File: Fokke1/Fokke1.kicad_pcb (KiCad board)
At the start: 2 copper layers, 209 x 64 mm, 97 parts, among them J1 Conn_02x20_Top_Bottom, SW1 SW_SPST, SW10 SW_SPST, SW11 SW_SPST, SW12 SW_SPST, SW2 SW_SPST, SW3 SW_SPST, SW4 SW_SPST, SW5 SW_SPST, SW6 SW_SPST, SW7 SW_SPST, SW8 SW_SPST, SW9 SW_SPST

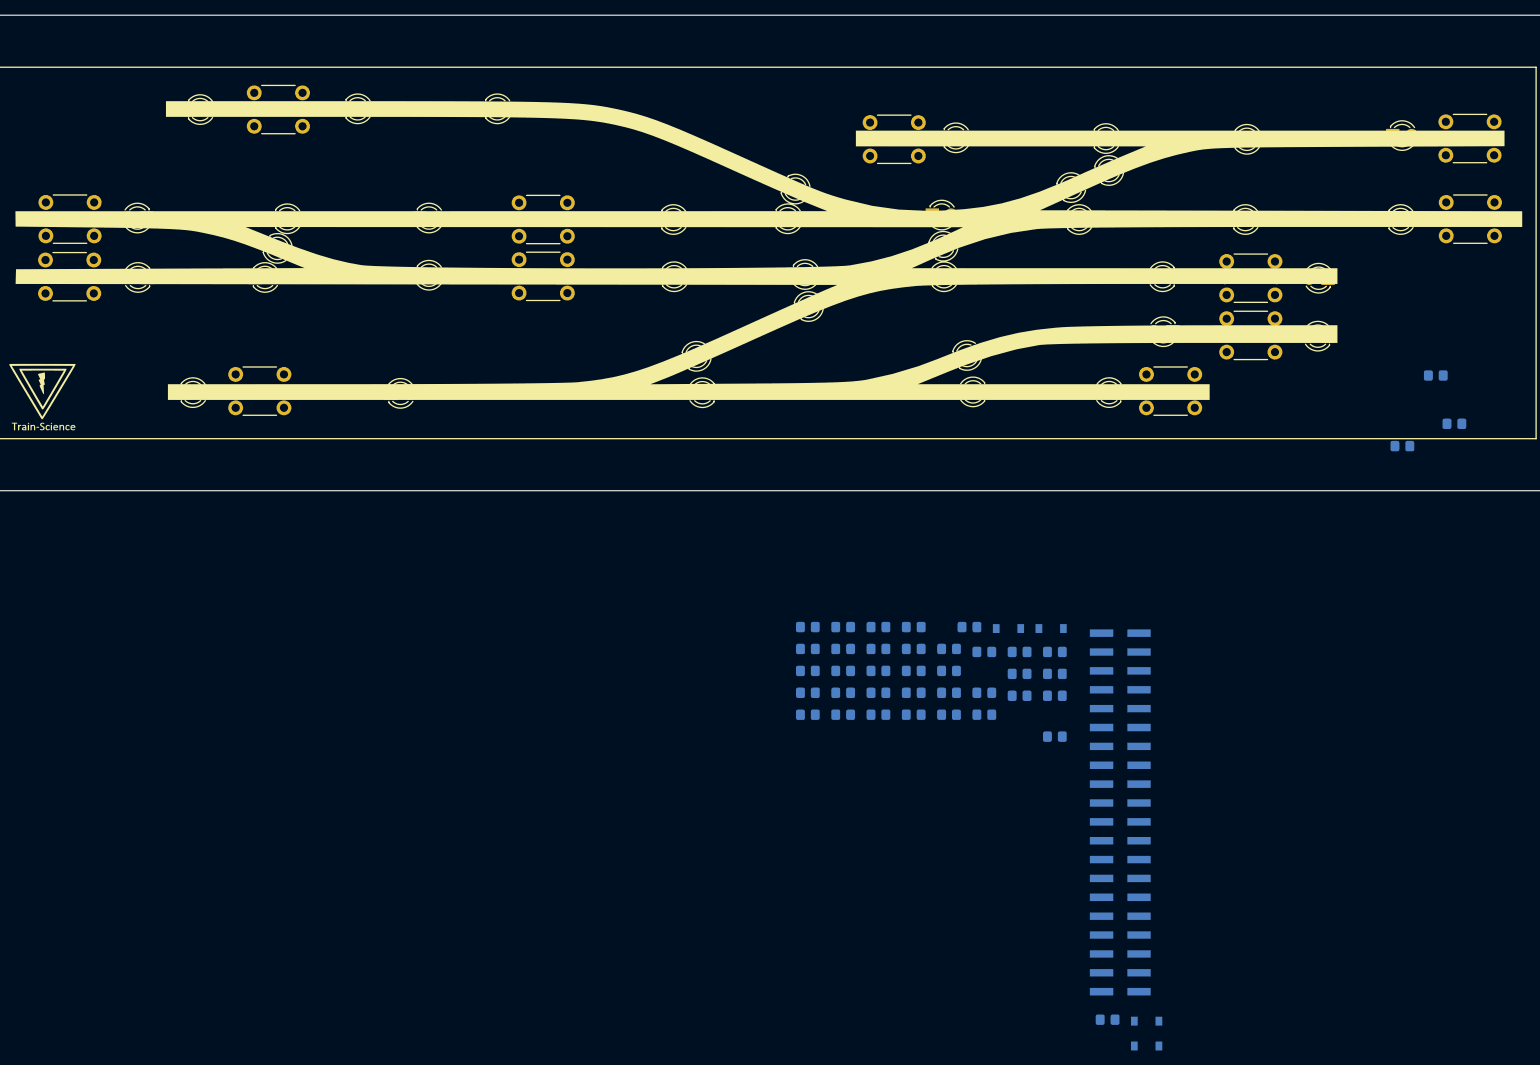
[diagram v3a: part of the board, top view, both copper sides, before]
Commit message: routed all but the main connector of Fokke1
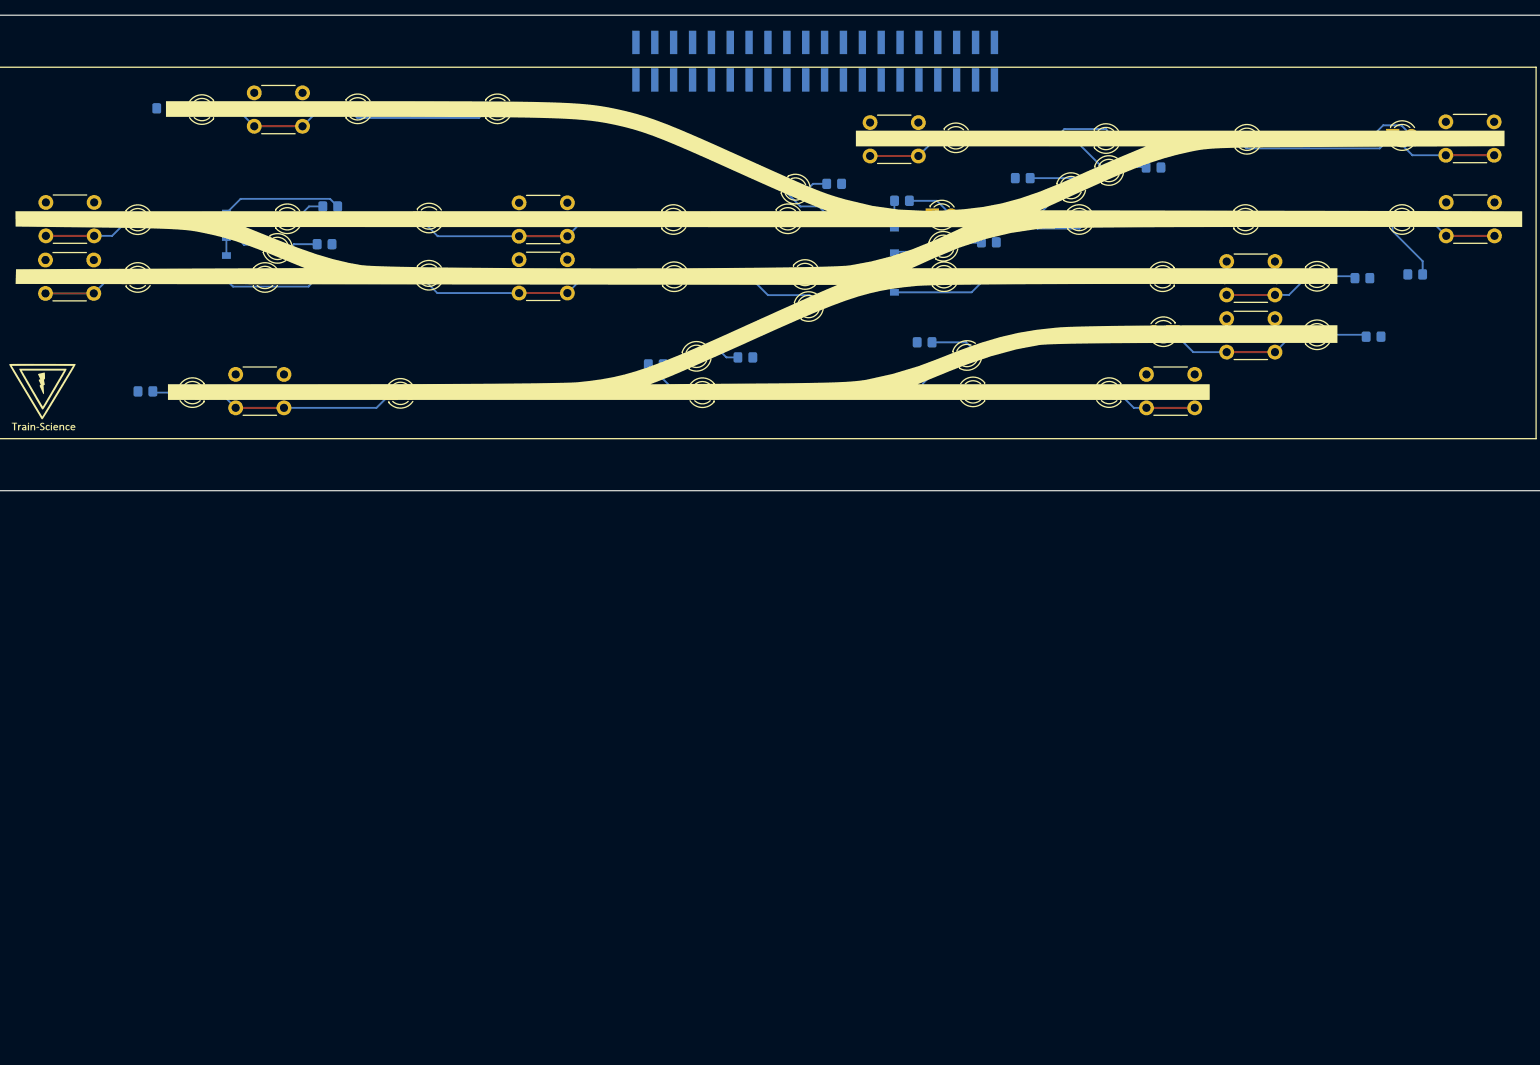
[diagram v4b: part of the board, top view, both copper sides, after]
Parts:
- moved R1 173.8 mm to (54.4, 96.5)
- moved D4 160.1 mm to (60.7, 103.0), turned to 90 degrees
- moved R31 126.2 mm to (52.3, 81.5), turned to 0 degrees
- moved R2 123.1 mm to (54.6, 104.4)
- moved R132 120.9 mm to (74.7, 94.7)
- moved D3 118.4 mm to (60.7, 97.3), turned to -90 degrees
- moved J1 109.1 mm to (140.0, 75.2), turned to -90 degrees
- moved D6 108.6 mm to (150.6, 104.6), turned to 90 degrees
- moved R152 105.0 mm to (118.5, 116.0)
- moved R41 104.6 mm to (49.8, 119.6), turned to 0 degrees
- moved R32 101.5 mm to (84.3, 81.5)
- moved R111 101.3 mm to (204.5, 85.9)
- moved R3 99.7 mm to (73.9, 99.8)
- moved R51 97.3 mm to (94.5, 96.3)
- moved R142 93.1 mm to (71.9, 104.4)
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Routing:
- net GPIO3: track 0.00 -> 40.1 mm
- net GPIO11: track 0.00 -> 36.9 mm
- net GPIO6: track 0.00 -> 34.9 mm
- net GPIO5: track 0.00 -> 34.8 mm
- net GPIO4: track 0.00 -> 27.1 mm
- net GPIO9: track 0.00 -> 20.3 mm
- net GPIO13: track 0.00 -> 16.2 mm
- net GPIO19: track 0.00 -> 13.5 mm
- net GPIO14: track 0.00 -> 13.0 mm
- net GPIO12: track 0.00 -> 12.1 mm
- net GPIO2: track 0.00 -> 12.0 mm
- net GPIO1: track 0.00 -> 12.0 mm
- net GPIO8: track 0.00 -> 11.9 mm
- net GPIO7: track 0.00 -> 11.3 mm
- net GPIO10: track 0.00 -> 11.1 mm
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
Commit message: commit 4 push
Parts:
- added C11: 100n, Capacitor_SMD:C_0603_1608Metric_Pad1.08x0.95mm_HandSolder, F.Cu at (276.3, 60.2)
- added C12: 100nF, Capacitor_SMD:C_0603_1608Metric_Pad1.08x0.95mm_HandSolder, F.Cu at (274.3, 72.8)
- added C13: 12pF, Capacitor_SMD:C_0402_1005Metric_Pad0.74x0.62mm_HandSolder, F.Cu at (104.9, 46.3)
- added C13: 12pF, Capacitor_SMD:C_0402_1005Metric_Pad0.74x0.62mm_HandSolder, F.Cu at (265.6, 58.9)
- added C14: 12pF, Capacitor_SMD:C_0402_1005Metric_Pad0.74x0.62mm_HandSolder, F.Cu at (108.7, 50.4)
- added C14: 12pF, Capacitor_SMD:C_0402_1005Metric_Pad0.74x0.62mm_HandSolder, F.Cu at (260.4, 59.4)
- added C29: 330nF, Capacitor_SMD:C_0603_1608Metric_Pad1.08x0.95mm_HandSolder, F.Cu at (282.4, 72.9)
- added C30: 100nF, Capacitor_SMD:C_0603_1608Metric_Pad1.08x0.95mm_HandSolder, F.Cu at (278.4, 66.8)
- added C301: 100n, Capacitor_SMD:C_0603_1608Metric_Pad1.08x0.95mm_HandSolder, F.Cu at (151.3, 36.5)
- added C31: 100uF, Capacitor_SMD:C_1206_3216Metric_Pad1.33x1.80mm_HandSolder, F.Cu at (279.0, 64.8)
- added C501: 1uF, Capacitor_SMD:C_0603_1608Metric_Pad1.08x0.95mm_HandSolder, F.Cu at (279.8, 62.4)
- added C501: 100nF, Capacitor_SMD:C_0603_1608Metric_Pad1.08x0.95mm_HandSolder, F.Cu at (172.7, 18.8)
- added C502: 1uF, Capacitor_SMD:C_0603_1608Metric_Pad1.08x0.95mm_HandSolder, F.Cu at (279.8, 57.0)
- added C601: 330nF, Capacitor_SMD:C_0603_1608Metric_Pad1.08x0.95mm_HandSolder, F.Cu at (168.0, 30.0)
- added C602: 100nF, Capacitor_SMD:C_0603_1608Metric_Pad1.08x0.95mm_HandSolder, F.Cu at (160.5, 30.0)
- added C603: 100uF, Capacitor_SMD:C_1206_3216Metric_Pad1.33x1.80mm_HandSolder, F.Cu at (158.0, 29.3)
- added C701: 12pF, Capacitor_SMD:C_0805_2012Metric_Pad1.18x1.45mm_HandSolder, F.Cu at (232.0, 30.4)
- added C701: 12pF, Capacitor_SMD:C_0805_2012Metric_Pad1.18x1.45mm_HandSolder, F.Cu at (189.6, 29.4)
- added C702: 12pF, Capacitor_SMD:C_0805_2012Metric_Pad1.18x1.45mm_HandSolder, F.Cu at (183.6, 29.4)
- added C702: 12pF, Capacitor_SMD:C_0805_2012Metric_Pad1.18x1.45mm_HandSolder, F.Cu at (226.0, 30.4)
- added D11: LED, LED_SMD:LED_0805_2012Metric_Pad1.15x1.40mm_HandSolder, F.Cu at (104.8, 38.9)
- added D11: LED, LED_SMD:LED_0805_2012Metric_Pad1.15x1.40mm_HandSolder, F.Cu at (256.0, 69.9)
- added J11: Conn_01x05_Male, custom_kicad_lib_sk:castellated_2.54mm_01x06, F.Cu at (284.8, 64.6)
- added J12: Conn_01x05_Male, custom_kicad_lib_sk:castellated_2.54mm_01x06, F.Cu at (249.3, 62.0)
- added J201: Conn_01x04_Male, Connector_PinHeader_2.54mm:PinHeader_1x04_P2.54mm_Horizontal, F.Cu at (199.1, 25.4)
- added J202: Conn_01x04_Female, Connector_PinSocket_2.54mm:PinSocket_1x04_P2.54mm_Horizontal, F.Cu at (184.5, 25.5)
- added J202: Conn_01x04_Female, Connector_PinSocket_2.54mm:PinSocket_1x04_P2.54mm_Horizontal, F.Cu at (228.5, 25.4)
- added J301: RJ12, Connector_RJ:RJ25_Wayconn_MJEA-660X1_Horizontal, F.Cu at (153.9, 27.5)
- added J401: Conn_02x08_Counter_Clockwise, Connector_IDC:IDC-Header_2x08_P2.54mm_Vertical, F.Cu at (181.1, 36.7)
- added J401: Conn_02x08_Counter_Clockwise, Connector_IDC:IDC-Header_2x08_P2.54mm_Vertical, F.Cu at (225.5, 36.7)
- added J401: Conn_01x10_Male, custom_kicad_lib_sk:castellated_2.54mm_01x10, F.Cu at (267.1, 53.2)
- added J403: Conn_01x10_Male, custom_kicad_lib_sk:castellated_2.54mm_01x10, F.Cu at (267.1, 76.0)
- added JP501: SolderJumper_3_Bridged12, Jumper:SolderJumper-3_P1.3mm_Bridged12_RoundedPad1.0x1.5mm_NumberLabels, B.Cu at (169.4, 31.3)
- added JP502: SolderJumper_3_Bridged12, Jumper:SolderJumper-3_P1.3mm_Bridged12_RoundedPad1.0x1.5mm_NumberLabels, B.Cu at (166.6, 31.3)
- added JP503: SolderJumper_3_Bridged12, Jumper:SolderJumper-3_P1.3mm_Bridged12_RoundedPad1.0x1.5mm_NumberLabels, B.Cu at (163.8, 31.3)
- added R11: 10k, Resistor_SMD:R_0402_1005Metric_Pad0.72x0.64mm_HandSolder, F.Cu at (120.7, 42.0)
- added R11: 10k, Resistor_SMD:R_0402_1005Metric_Pad0.72x0.64mm_HandSolder, F.Cu at (256.7, 65.8)
- added R12: 6k2, Resistor_SMD:R_0603_1608Metric_Pad0.98x0.95mm_HandSolder, F.Cu at (256.2, 68.0)
- added R12: 6k2, Resistor_SMD:R_0603_1608Metric_Pad0.98x0.95mm_HandSolder, F.Cu at (104.6, 40.9)
- added R13: 10k, Resistor_SMD:R_0402_1005Metric_Pad0.72x0.64mm_HandSolder, F.Cu at (254.2, 65.8)
- added R13: 10k, Resistor_SMD:R_0402_1005Metric_Pad0.72x0.64mm_HandSolder, F.Cu at (120.7, 39.5)
- added R201: R, Resistor_SMD:R_0805_2012Metric_Pad1.20x1.40mm_HandSolder, F.Cu at (165.3, 25.3)
- added R201: R, Resistor_SMD:R_0805_2012Metric_Pad1.20x1.40mm_HandSolder, F.Cu at (206.5, 21.9)
- added R202: 6k2, Resistor_SMD:R_0805_2012Metric_Pad1.20x1.40mm_HandSolder, F.Cu at (161.5, 25.3)
- added R202: 6k2, Resistor_SMD:R_0805_2012Metric_Pad1.20x1.40mm_HandSolder, F.Cu at (206.5, 26.9)
- added R301: 10k, Resistor_SMD:R_0402_1005Metric, F.Cu at (157.0, 41.3)
- added R301: 10k, Resistor_SMD:R_0402_1005Metric, F.Cu at (268.5, 59.0)
- added R302: 10k, Resistor_SMD:R_0402_1005Metric, F.Cu at (268.5, 58.0)
- added R302: 10k, Resistor_SMD:R_0402_1005Metric, F.Cu at (155.3, 41.3)
- added R303: 10k, Resistor_SMD:R_0402_1005Metric, F.Cu at (153.5, 41.3)
- added R303: 10k, Resistor_SMD:R_0402_1005Metric, F.Cu at (268.5, 60.0)
- added R501: 4k7, Resistor_SMD:R_0603_1608Metric, F.Cu at (158.7, 19.6)
- added R502: 4k7, Resistor_SMD:R_0603_1608Metric, F.Cu at (169.1, 19.5)
- added R601: 4k7, Resistor_SMD:R_0603_1608Metric, F.Cu at (270.0, 72.8)
- added R602: 4k7, Resistor_SMD:R_0603_1608Metric, F.Cu at (281.1, 74.9)
- added R702: 10k, Resistor_SMD:R_0603_1608Metric_Pad0.98x0.95mm_HandSolder, F.Cu at (232.5, 33.9)
- added R702: 10k, Resistor_SMD:R_0603_1608Metric_Pad0.98x0.95mm_HandSolder, F.Cu at (188.7, 33.9)
- added REF**: PinHeader_1x08_P1.27mm_Vertical, Connector_PinHeader_1.27mm:PinHeader_1x08_P1.27mm_Vertical, F.Cu at (113.2, 52.9)
- added REF**: PinHeader_1x08_P1.27mm_Vertical, Connector_PinHeader_1.27mm:PinHeader_1x08_P1.27mm_Vertical, F.Cu at (104.2, 52.9)
- added REF**: MountingHole_3.2mm_M3, MountingHole:MountingHole_3.2mm_M3, F.Cu at (146.2, 39.2)
- added REF**: MountingHole_3.2mm_M3, MountingHole:MountingHole_3.2mm_M3, F.Cu at (198.5, 39.4)
- added REF**: MountingHole_3.2mm_M3, MountingHole:MountingHole_3.2mm_M3, F.Cu at (191.2, 39.4)
- added REF**: PinHeader_1x08_P1.27mm_Vertical, Connector_PinHeader_1.27mm:PinHeader_1x08_P1.27mm_Vertical, F.Cu at (113.2, 35.4)
- added REF**: MountingHole_3.2mm_M3, MountingHole:MountingHole_3.2mm_M3, F.Cu at (235.0, 39.4)
- added REF**: PinHeader_1x08_P1.27mm_Vertical, Connector_PinHeader_1.27mm:PinHeader_1x08_P1.27mm_Vertical, F.Cu at (104.2, 35.4)
- added SW11: SW_SPST, Button_Switch_SMD:SW_SPST_SKQG_WithStem, F.Cu at (255.0, 60.8)
- added U11: MAX485E, Package_SO:SOIC-8_3.9x4.9mm_P1.27mm, F.Cu at (272.7, 60.0)
- added U12: 24LC256, Package_SO:SOIC-8_3.9x4.9mm_P1.27mm, F.Cu at (273.0, 68.3)
- added U13: ATmega328-A, Package_QFP:TQFP-32_7x7mm_P0.8mm, F.Cu at (264.0, 66.5)
- added U13: ATmega328-A, Package_QFP:TQFP-32_7x7mm_P0.8mm, F.Cu at (112.8, 43.7)
- added U14: HEADER_3x2, Connector_PinSocket_1.27mm:PinSocket_2x03_P1.27mm_Vertical, F.Cu at (251.3, 74.4)
- added U14: HEADER_3x2, Connector_PinSocket_1.27mm:PinSocket_2x03_P1.27mm_Vertical, F.Cu at (121.0, 47.1)
- added U26: L78L05_SOT89, Package_TO_SOT_SMD:SOT-89-3, F.Cu at (279.0, 70.3)
- added U301: MAX485E, Package_SO:SOIC-8_3.9x4.9mm_P1.27mm, F.Cu at (155.1, 36.4)
- added U501: XC6206PxxxMR, Package_TO_SOT_SMD:SOT-23, F.Cu at (279.5, 59.7)
- added U501: 24LC256, Package_SO:SOIC-8_3.9x4.9mm_P1.27mm, F.Cu at (164.0, 20.4)
- added U601: L78L05_SOT89, Package_TO_SOT_SMD:SOT-89-3, F.Cu at (164.3, 29.3)
- added U701: ATmega328-A, Package_QFP:TQFP-32_7x7mm_P0.8mm, F.Cu at (174.9, 26.5)
- added U701: ATmega328-A, Package_QFP:TQFP-32_7x7mm_P0.8mm, F.Cu at (215.5, 24.9)
- added U702: HEADER_3x2, Connector_PinSocket_1.27mm:PinSocket_2x03_P1.27mm_Vertical, F.Cu at (192.1, 34.2)
- added U702: HEADER_3x2, Connector_PinSocket_1.27mm:PinSocket_2x03_P1.27mm_Vertical, F.Cu at (235.9, 34.2)
- added Y11: crystal_arduino, custom_kicad_lib_sk:crystal_arduino, F.Cu at (262.9, 59.3)
- added Y11: crystal_arduino, custom_kicad_lib_sk:crystal_arduino, F.Cu at (107.2, 47.9)
- added Y701: crystal_arduino, custom_kicad_lib_sk:crystal_arduino, F.Cu at (186.5, 29.4)
- added Y701: crystal_arduino, custom_kicad_lib_sk:crystal_arduino, F.Cu at (228.8, 30.4)
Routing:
- net (no net): track 0.00 -> 334.7 mm, vias 0 -> 19
- net GPIO11: track 36.9 -> 55.7 mm
- net GPIO2: track 12.0 -> 30.8 mm, vias 0 -> 2
- net GPIO6: track 34.9 -> 51.4 mm
- net GPIO5: track 34.8 -> 51.1 mm
- net GPIO13: track 16.2 -> 32.1 mm, vias 0 -> 2
- net GPIO9: track 20.3 -> 35.9 mm, vias 0 -> 2
- net GPIO7: track 11.3 -> 26.9 mm
- net GPIO8: track 11.9 -> 26.6 mm
- net GPIO12: track 12.1 -> 25.4 mm, vias 0 -> 2
- net GPIO3: track 40.1 -> 52.8 mm
- net GPIO4: track 27.1 -> 37.9 mm
- net GPIO10: track 11.1 -> 20.4 mm
- net +3V3: track 0.00 -> 8.18 mm
- net GND: track 0.00 -> 7.62 mm, vias 0 -> 36
- added copper zone on B.Cu, net GND
- added copper zone on F.Cu, net GND
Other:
- board size 209 x 64 mm -> 255.9 x 116.6 mm
- board text added: "3V3"
- board text added: "5V"
- board text added: "A"
- board text added: "A0"
- board text added: "A1"
- board text added: "A2"
- board text added: "A3"
- board text added: "B"
- board text added: "D10"
- board text added: "D11"
- board text added: "D12"
- board text added: "D13"
- board text added: "D2"
- board text added: "D3"
- board text added: "D4"
- board text added: "D5"
- board text added: "D6"
- board text added: "D7"
- board text added: "D8"
- board text added: "D9"
- board text added: "GND"
- board text added: "ICSP"
- board text added: "RES"
- board text added: "RX"
- board text added: "SCL"
- board text added: "SDA"
- board text added: "TX"
- board text added: "Train-Science"
- board text added: "Vin"

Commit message: I added a button to Fokke 1 for his gate, but I lost annonation with the schematic. The schematic as is now is FUBAR. The project however is finished so I got lucky...
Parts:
- removed C11, C301: 100n, Capacitor_SMD:C_0603_1608Metric_Pad1.08x0.95mm_HandSolder
- removed C12, C30, C501, C602: 100nF, Capacitor_SMD:C_0603_1608Metric_Pad1.08x0.95mm_HandSolder
- removed C13 (x2), C14 (x2): 12pF, Capacitor_SMD:C_0402_1005Metric_Pad0.74x0.62mm_HandSolder
- removed C29, C601: 330nF, Capacitor_SMD:C_0603_1608Metric_Pad1.08x0.95mm_HandSolder
- removed C31, C603: 100uF, Capacitor_SMD:C_1206_3216Metric_Pad1.33x1.80mm_HandSolder
- removed C501, C502: 1uF, Capacitor_SMD:C_0603_1608Metric_Pad1.08x0.95mm_HandSolder
- removed C701 (x2), C702 (x2): 12pF, Capacitor_SMD:C_0805_2012Metric_Pad1.18x1.45mm_HandSolder
- removed D11 (x2): LED, LED_SMD:LED_0805_2012Metric_Pad1.15x1.40mm_HandSolder
- removed J11, J12: Conn_01x05_Male, custom_kicad_lib_sk:castellated_2.54mm_01x06
- removed J201: Conn_01x04_Male, Connector_PinHeader_2.54mm:PinHeader_1x04_P2.54mm_Horizontal
- removed J202 (x2): Conn_01x04_Female, Connector_PinSocket_2.54mm:PinSocket_1x04_P2.54mm_Horizontal
- removed J301: RJ12, Connector_RJ:RJ25_Wayconn_MJEA-660X1_Horizontal
- removed J401 (x2): Conn_02x08_Counter_Clockwise, Connector_IDC:IDC-Header_2x08_P2.54mm_Vertical
- removed J401, J403: Conn_01x10_Male, custom_kicad_lib_sk:castellated_2.54mm_01x10
- removed JP501, JP502, JP503: SolderJumper_3_Bridged12, Jumper:SolderJumper-3_P1.3mm_Bridged12_RoundedPad1.0x1.5mm_NumberLabels
- removed R11 (x2), R13 (x2): 10k, Resistor_SMD:R_0402_1005Metric_Pad0.72x0.64mm_HandSolder
- removed R12 (x2): 6k2, Resistor_SMD:R_0603_1608Metric_Pad0.98x0.95mm_HandSolder
- removed the R201 at (165.3, 25.3)
- removed the R201 at (206.5, 21.9)
- removed the R202 at (161.5, 25.3)
- removed the R202 at (206.5, 26.9)
- removed R301 (x2), R302 (x2), R303 (x2): 10k, Resistor_SMD:R_0402_1005Metric
- removed R501, R502, R601, R602: 4k7, Resistor_SMD:R_0603_1608Metric
- removed R702 (x2): 10k, Resistor_SMD:R_0603_1608Metric_Pad0.98x0.95mm_HandSolder
- removed the REF** at (113.2, 52.9)
- removed the REF** at (104.2, 52.9)
- removed the REF** at (146.2, 39.2)
- removed the REF** at (198.5, 39.4)
- removed the REF** at (191.2, 39.4)
- removed the REF** at (113.2, 35.4)
- removed the REF** at (235.0, 39.4)
- removed the REF** at (104.2, 35.4)
- removed the SW11 at (255.0, 60.8)
- removed U11, U301: MAX485E, Package_SO:SOIC-8_3.9x4.9mm_P1.27mm
- removed U12, U501: 24LC256, Package_SO:SOIC-8_3.9x4.9mm_P1.27mm
- removed U13 (x2), U701 (x2): ATmega328-A, Package_QFP:TQFP-32_7x7mm_P0.8mm
- removed U14 (x2), U702 (x2): HEADER_3x2, Connector_PinSocket_1.27mm:PinSocket_2x03_P1.27mm_Vertical
- removed U26, U601: L78L05_SOT89, Package_TO_SOT_SMD:SOT-89-3
- removed U501: XC6206PxxxMR, Package_TO_SOT_SMD:SOT-23
- removed Y11 (x2), Y701 (x2): crystal_arduino, custom_kicad_lib_sk:crystal_arduino
- added J2: 6P6C, Connector_RJ:RJ12_Amphenol_54601, B.Cu at (40.2, 71.6)
- added J3: panelX_controller, custom_kicad_lib_sk:panelX_contoller, B.Cu at (152.3, 86.1)
- added R101: 100R, Resistor_SMD:R_0805_2012Metric_Pad1.20x1.40mm_HandSolder, B.Cu at (158.2, 71.4)
- added REF**: MountingHole_3.2mm_M3, MountingHole:MountingHole_3.2mm_M3, F.Cu at (98.3, 129.5)
- added REF**: MountingHole_3.2mm_M3, MountingHole:MountingHole_3.2mm_M3, F.Cu at (231.4, 72.5)
- added REF**: MountingHole_3.2mm_M3, MountingHole:MountingHole_3.2mm_M3, F.Cu at (48.9, 72.5)
- added REF**: MountingHole_3.2mm_M3, MountingHole:MountingHole_3.2mm_M3, F.Cu at (37.2, 129.4)
- added REF**: MountingHole_3.2mm_M3, MountingHole:MountingHole_3.2mm_M3, F.Cu at (232.8, 129.5)
- added REF**: MountingHole_3.2mm_M3, MountingHole:MountingHole_3.2mm_M3, F.Cu at (97.3, 72.5)
- added REF**: MountingHole_3.2mm_M3, MountingHole:MountingHole_3.2mm_M3, F.Cu at (178.1, 129.5)
- added REF**: MountingHole_3.2mm_M3, MountingHole:MountingHole_3.2mm_M3, F.Cu at (174.0, 72.5)
- added SW30: SW_SPST, custom_kicad_lib_sk:SW_NO_SILK, F.Cu at (59.8, 112.9)
- D4, D5: value D -> LED; footprint Diode_SMD:D_SOD-123 -> custom_kicad_lib_sk:LED_NO_SILK
- J1: value Conn_02x20_Top_Bottom -> panelX_controller; footprint Connector_PinHeader_2.54mm:PinHeader_2x20_P2.54mm_Vertical_SMD -> custom_kicad_lib_sk:panelX_contoller
- R1, R10, R32: value 1k5 -> 3k3
- moved J1 22.8 mm to (119.9, 86.0), turned to 180 degrees
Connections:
- D1 pad 1: GPIO1 -> GND
- D10 pad 1: GPIO10 -> GPIO3
- D111 pad 1: GPIO11 -> GPIO22
- D112 pad 1: GPIO11 -> GPIO22
- D121 pad 1: GPIO12 -> GPIO21
- D122 pad 1: GPIO12 -> GPIO21
- D151 pad 1: GPIO15 -> GPIO9
- D161 pad 1: GPIO16 -> GPIO11
- D171 pad 1: GPIO17 -> GPIO10
- D2 pad 1: GPIO2 -> GPIO1
- D201 pad 1: GPIO20 -> GPIO16
- D211 pad 1: GPIO21 -> GPIO12
- D221 pad 1: GPIO22 -> GPIO17
- D3 pad 1: GPIO13 -> GPIO4
- D3 pad 2: Net-(D1314-Pad1) -> Net-(D3-Pad2)
- D31 pad 1: GPIO3 -> GPIO16
- D32 pad 1: GPIO3 -> GND
- D33 pad 1: GPIO3 -> GPIO19
- D4 pad 1: GPIO14 -> Net-(D3-Pad2)
- D4 pad 2: Net-(D1314-Pad1) -> Net-(D4-Pad2)
- D41 pad 1: GPIO4 -> GPIO22
- D42 pad 1: GPIO4 -> GPIO21
- D5 pad 1: GPIO18 -> GPIO2
- D5 pad 2: Net-(D1819-Pad1) -> Net-(D5-Pad2)
- D51 pad 1: GPIO5 -> GPIO7
- D52 pad 1: GPIO5 -> GPIO7
- D6 pad 1: GPIO19 -> GPIO5
- D6 pad 2: Net-(D1819-Pad1) -> Net-(D3-Pad2)
- D61 pad 1: GPIO6 -> GPIO8
- D62 pad 1: GPIO6 -> GPIO8
- D7 pad 1: GPIO7 -> GND
- D81 pad 1: GPIO8 -> GPIO20
- D82 pad 1: GPIO8 -> GPIO20
- D91 pad 1: GPIO9 -> GPIO19
- D92 pad 1: GPIO9 -> GPIO19
- J1 pad 1: unconnected-(J1-Pad1) -> +3V3
- J1 pad 10: unconnected-(J1-Pad10) -> GND
- J1 pad 11: unconnected-(J1-Pad11) -> GPIO11
- J1 pad 13: unconnected-(J1-Pad13) -> GPIO10
- J1 pad 14: unconnected-(J1-Pad14) -> SCL
- J1 pad 15: unconnected-(J1-Pad15) -> GPIO9
- J1 pad 16: unconnected-(J1-Pad16) -> SDA
- J1 pad 17: unconnected-(J1-Pad17) -> GPIO7
- J1 pad 18: unconnected-(J1-Pad18) -> GPIO8
- J1 pad 19: unconnected-(J1-Pad19) -> GPIO5
- J1 pad 2: unconnected-(J1-Pad2) -> +5V
- J1 pad 20: unconnected-(J1-Pad20) -> GPIO6
- J1 pad 21: unconnected-(J1-Pad21) -> GPIO3
- J1 pad 22: unconnected-(J1-Pad22) -> GPIO4
- J1 pad 23: unconnected-(J1-Pad23) -> GPIO1
- J1 pad 24: unconnected-(J1-Pad24) -> GPIO2
- J1 pad 3: unconnected-(J1-Pad3) -> GPIO15
- J1 pad 4: unconnected-(J1-Pad4) -> +12V
- J1 pad 5: unconnected-(J1-Pad5) -> GPIO14
- J1 pad 6: unconnected-(J1-Pad6) -> Net-(J1-Pad6)
- J1 pad 7: unconnected-(J1-Pad7) -> GPIO13
- J1 pad 8: unconnected-(J1-Pad8) -> Net-(J1-Pad8)
- J1 pad 9: unconnected-(J1-Pad9) -> GPIO12
- R1 pad 1: +3V3 -> GPIO4
- R10 pad 1: +3V3 -> GPIO9
- R10 pad 2: Net-(D10-Pad2) -> Net-(D12-Pad2)
- R132 pad 1: GPIO13 -> GPIO4
- R142 pad 1: GPIO14 -> GPIO5
- R152 pad 1: GPIO15 -> GPIO9
- R162 pad 1: GPIO16 -> GPIO11
- R172 pad 1: GPIO17 -> GPIO10
- R182 pad 1: GPIO18 -> GPIO14
- R192 pad 1: GPIO19 -> GPIO13
- R202 pad 1: GPIO20 -> GPIO16
- R212 pad 1: GPIO21 -> GPIO12
- R222 pad 1: GPIO22 -> GPIO17
- R3 pad 2: Net-(D1314-Pad2) -> Net-(D4-Pad2)
- R31 pad 2: Net-(D31-Pad2) -> Net-(D34-Pad2)
- R32 pad 1: +3V3 -> GPIO12
- R32 pad 2: Net-(D32-Pad2) -> Net-(D35-Pad2)
- R33 pad 2: Net-(D33-Pad2) -> Net-(D36-Pad2)
- R7 pad 2: Net-(D7-Pad2) -> Net-(D9-Pad2)
- SW10 pad 2: GPIO10 -> GPIO18
- SW11 pad 2: GPIO11 -> GPIO22
- SW12 pad 2: GPIO12 -> GPIO21
- SW4 pad 2: GPIO4 -> GPIO6
- SW5 pad 2: GPIO5 -> GPIO7
- SW6 pad 2: GPIO6 -> GPIO8
- SW7 pad 2: GPIO7 -> GPIO23
- SW8 pad 2: GPIO8 -> GPIO20
- SW9 pad 2: GPIO9 -> GPIO19
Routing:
- net +3V3: track 8.18 -> 598.6 mm, vias 0 -> 20
- net (no net): track 334.7 -> 0.00 mm, vias 19 -> 0
- net GPIO30: track 0.00 -> 177.9 mm
- net +12V: track 0.00 -> 133.4 mm
- net GPIO21: track 7.18 -> 139.3 mm
- net GPIO18: track 3.69 -> 98.6 mm
- net Net-(J1-Pad6): track 0.00 -> 94.1 mm, vias 0 -> 1
- net Net-(J1-Pad8): track 0.00 -> 92.3 mm
- net GPIO19: track 13.5 -> 101.9 mm
- net GPIO22: track 6.63 -> 91.6 mm
- net GPIO20: track 4.59 -> 86.9 mm
- net GPIO1: track 12.0 -> 89.7 mm
- net GPIO2: track 30.8 -> 103.3 mm, vias 2 -> 0
- net GPIO6: track 51.4 -> 114.0 mm
- net GPIO17: track 3.37 -> 51.4 mm
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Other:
- board size 255.9 x 116.6 mm -> 209 x 64 mm
- board text added: "101a"
- board text added: "103b"
- board text added: "105a"
- board text added: "107b"
- board text added: "109"
- board text added: "111"
- board text added: "113"
- board text added: "115"
- board text added: "117"
- board text added: "119"
- board text added: "2A"
- board text added: "3A"
- board text added: "3B"
- board text added: "Bs >>"
- board text added: "VAM"
- board text removed: "3V3"
- board text removed: "5V"
- board text removed: "A"
- board text removed: "A0"
- board text removed: "A1"
- board text removed: "A2"
- board text removed: "A3"
- board text removed: "B"
- board text removed: "D10"
- board text removed: "D11"
- board text removed: "D12"
- board text removed: "D13"
- board text removed: "D2"
- board text removed: "D3"
- board text removed: "D4"
- board text removed: "D5"
- board text removed: "D6"
- board text removed: "D7"
- board text removed: "D8"
- board text removed: "D9"
- board text removed: "GND"
- board text removed: "ICSP"
- board text removed: "RES"
- board text removed: "RX"
- board text removed: "SCL"
- board text removed: "SDA"
- board text removed: "TX"
- board text removed: "Train-Science"
- board text removed: "Vin"
